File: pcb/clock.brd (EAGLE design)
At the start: 145 x 50 mm, 72 parts, among them IC1 STM32F072C8T6, IC2 REG1117, IC3 24C64ST, U1 DS18B20, X3 USB-MICROB

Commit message: added bom
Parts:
- removed C10, C4, C5, C9: (no value), clock:C1210
- C1, C6, C7, C8: value (none) -> 100nF
- C11, C12: value (none) -> 20p
- C13, C14, C2: value (none) -> 47uF
- C17, C3: value (none) -> 20pF
- L1: value (none) -> 33nH
- R1, R13, R16, R17, R2, R3, R7, R8, R9: value (none) -> 4K7
- R11, R12, R4: value (none) -> 10
- R14, R15, R5: value (none) -> 100
- X2: value (none) -> 32.768KHz
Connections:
- net +3V3: no longer C10.1, C4.1, C5.1, C9.1
- net GND: no longer C10.2, C4.2, C5.2, C9.2
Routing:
- net +3V3: track 78.4 -> 70.3 mm, vias 18 -> 14

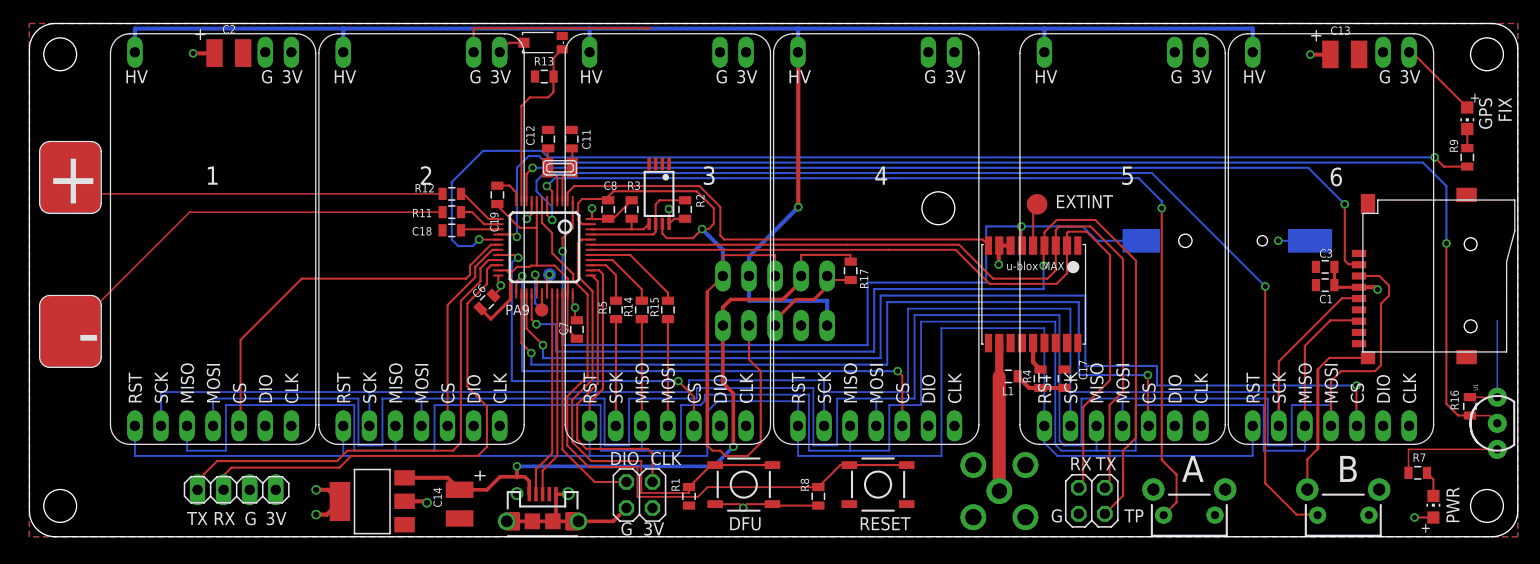
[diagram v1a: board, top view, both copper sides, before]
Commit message: updated to USBC connector
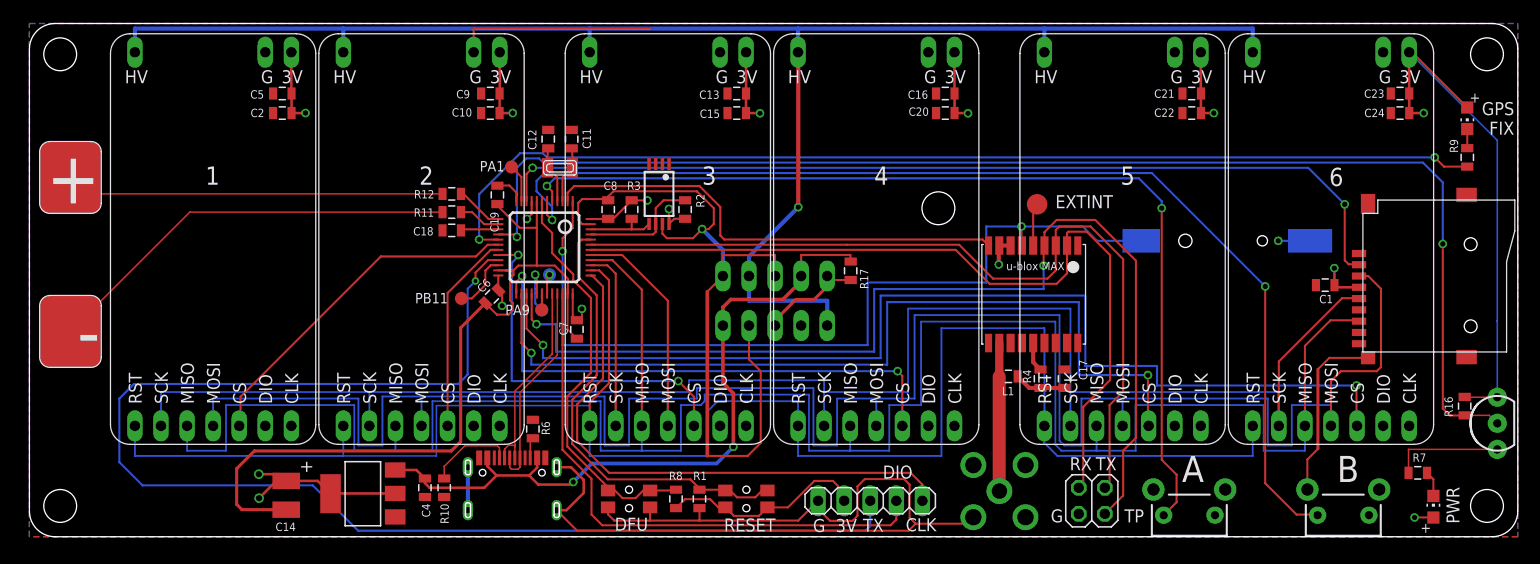
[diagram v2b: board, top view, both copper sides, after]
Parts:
- removed C3: 20pF, clock:0805
- removed JP3: (no value), pinhead:2X02
- removed JP5: (no value), pinhead:1X04
- removed R13: 4K7, clock:0805
- removed R14, R15, R5: 100, clock:0805
- removed S1, S2: TAC_SWITCHSMD, SparkFun-Retired:TACTILE-SWITCH-SMD
- removed U$8: TEMT6000, ProtoSnap-v14a:TEMT6000-SEN
- removed X3: USB-MICROB, basicBoard:USB-MICROB
- added C10, C15, C20, C22, C24, C4, C5: 100nF, clock:0805
- added C16, C21, C23, C9: 10uF, clock:0805
- added JP6: (no value), pinhead:1X05
- added R10, R6: 5.1K, joyAnalog:0805
- added SW1, SW4: 324_SW324_SWITCH_FOOT_HOLE, 3pos_slide_switch:342_SWICH_FOOT_HOLE
- added TP5, TP6: TEST-POINT3X5, SparkFun-Passives:PAD.03X.05
- added U2: USBC_16P, my_usbc_16p:USBC_16P_FOOT
- C13, C2: value 47uF -> 10uF; device clock:C1210 -> clock:0805
- moved C13 59.4 mm to (68.9, 43.2), turned to 180 degrees
- moved C14 16.9 mm to (25.0, 4.04)
- moved R8 13.9 mm to (63.0, 3.68)
- moved C2 7.83 mm to (24.6, 41.3), turned to 180 degrees
- moved IC2 1.19 mm to (32.5, 4.19)
- moved R1 1.05 mm to (65.3, 3.68)
- moved C6 0.72 mm to (45.1, 23.4)
- moved R16 0.51 mm to (139.8, 12.7)
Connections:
- removed net LIGHT_SENSOR_OUTPUT: IC1.11, R13.2, U$8.EMITTER
- removed net N$17: IC1.39, R5.1
- removed net N$19: IC1.41, R15.1
- removed net N$20: IC1.40, R14.1
- removed net PB10: IC1.21, JP5.1
- removed net PB11: IC1.22, JP5.2
- new net N$16: IC1.21, JP6.3
- new net N$22: IC1.22, TP5.P$1
- new net N$23: IC1.11, TP6.P$1
- new net N$31: R6.1, U2.B5
- new net N$33: R10.1, U2.A5
- net +3V3: now also C10.1, C14.1, C15.1, C16.1, C20.1, C21.1, C22.1, C23.1, C24.1, C5.1, C9.1, JP6.2, SW1.P$1, SW1.P$4; no longer C3.1, JP3.3, JP5.4, S1.3, S1.4, U$8.COLLECTOR
- net +5V: now also C4.1, U2.A4B9, U2.B4A9; no longer C14.1, X3.VBUS
- net GND: now also C10.2, C15.2, C16.2, C20.2, C21.2, C22.2, C23.2, C24.2, C4.2, C5.2, C9.2, JP6.1, R10.2, R6.2, SW4.P$1, SW4.P$4, U2.A1B12, U2.B11A12, U2.P$13, U2.P$14, U2.P$15, U2.P$16; no longer C3.2, JP3.1, JP5.3, R13.1, S2.3, S2.4, X3.GND, X3.P1, X3.P2, X3.P3, X3.P4, X3.P5, X3.P6
- net N$3: now also SW4.P$2, SW4.P$3; no longer S2.1, S2.2
- net N$5: now also SW1.P$2, SW1.P$3; no longer S1.1, S1.2
- net SPI1_MISO: now also IC1.40; no longer R14.2
- net SPI1_MOSI: now also IC1.41; no longer R15.2
- net SPI1_SCK: now also IC1.39; no longer R5.2
- net SWCLK: now also JP6.5; no longer JP3.4
- net SWDIO: now also JP6.4; no longer JP3.2
- net USB_DM: now also U2.A7, U2.B7; no longer X3.D-
- net USB_DP: now also U2.A6, U2.B6; no longer X3.D+
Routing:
- net N$16: track 0.00 -> 132.6 mm, vias 0 -> 1
- net GND: track 174.9 -> 302.3 mm
- net +3V3: track 70.3 -> 157.7 mm, vias 14 -> 16
- net PB11: track 48.3 -> 0.00 mm
- net PB10: track 47.9 -> 0.00 mm
- net SWDIO: track 22.8 -> 54.9 mm
- net SWCLK: track 27.9 -> 54.7 mm
- net N$3: track 64.6 -> 40.0 mm
- net LIGHT_SENSOR_OUTPUT: track 17.5 -> 0.00 mm
- net SPI1_MOSI: track 219.0 -> 229.6 mm
- net SPI1_MISO: track 210.1 -> 220.0 mm
- net N$19: track 9.82 -> 0.00 mm
- net N$33: track 0.00 -> 8.46 mm
- net EXIXE_RESET: track 171.5 -> 178.9 mm
- net N$20: track 7.27 -> 0.00 mm
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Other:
- board text added: "PA1"
- board text added: "PB11"
- board text added: "exixe clock PT3 JUL19 dekuNukem"

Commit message: moved header
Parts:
- moved JP6 3.30 mm to (78.6, 3.51)
- moved R8 1.63 mm to (61.4, 3.68)
- moved SW1 1.52 mm to (68.3, 3.68)
- moved SW4 1.52 mm to (56.9, 3.68)
- moved R1 1.45 mm to (63.8, 3.71)
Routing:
- net GND: track 302.3 -> 277.5 mm
- net SWCLK: track 54.7 -> 51.4 mm
- net N$16: track 132.6 -> 129.6 mm
- net SWDIO: track 54.9 -> 52.7 mm
- net N$5: track 44.3 -> 43.5 mm
- net N$3: track 40.0 -> 39.3 mm

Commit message: clean up
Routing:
- net EXIXE1_CS: track 34.1 -> 36.6 mm
- net GND: track 277.5 -> 276.2 mm
- net +3V3: track 157.3 -> 156.7 mm
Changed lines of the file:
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@@
 <text x="79.756" y="5.588" size="1.27" layer="25">DIO</text>
 <text x="85.471" y="1.778" size="1.27" layer="25" rot="R180">CLK</text>
-<text x="71.6534" y="1.7526" size="1.27" layer="25" rot="R180">RESET</text>
+<text x="71.3486" y="1.8034" size="1.27" layer="25" rot="R180">RESET</text>
 <text x="58.5724" y="1.8034" size="1.27" layer="25" rot="R180">DFU</text>
 <text x="100.711" y="2.667" size="1.27" layer="25" rot="R180">G</text>
@@
 <contactref element="SW4" pad="P$4"/>
 <contactref element="JP6" pad="1"/>
-<wire x1="78.0796" y1="5.6134" x2="81.915" y2="5.6134" width="0.2032" layer="1"/>
-<wire x1="78.0796" y1="5.6134" x2="77.3684" y2="4.9022" width="0.2032" layer="1"/>
+<wire x1="77.3684" y1="4.9022" x2="78.0796" y2="5.6134" width="0.2032" layer="1"/>
 <wire x1="77.3684" y1="2.032" x2="76.8858" y2="1.5494" width="0.2032" layer="1"/>
 <wire x1="76.8858" y1="1.5494" x2="74.7014" y2="1.5494" width="0.2032" layer="1"/>
@@
 <wire x1="91.96" y1="1.905" x2="90.6392" y2="0.5842" width="0.2032" layer="1"/>
 <wire x1="90.6392" y1="0.5842" x2="82.3976" y2="0.5842" width="0.2032" layer="1"/>
-<wire x1="79.8576" y1="0.5842" x2="53.3645" y2="0.5842" width="0.2032" layer="1"/>
+<wire x1="82.3976" y1="0.5842" x2="53.3645" y2="0.5842" width="0.2032" layer="1"/>
 <wire x1="81.915" y1="5.6134" x2="82.3976" y2="5.1308" width="0.2032" layer="1"/>
 <wire x1="82.3976" y1="5.1308" x2="82.3976" y2="0.5842" width="0.2032" layer="1"/>
 <wire x1="61.666" y1="30.476" x2="61.666" y2="29.52" width="0.2032" layer="1"/>
-<wire x1="78.0796" y1="5.6134" x2="79.375" y2="5.6134" width="0.2032" layer="1"/>
-<wire x1="82.3976" y1="0.5842" x2="79.8576" y2="0.5842" width="0.2032" layer="1"/>
+<wire x1="78.0796" y1="5.6134" x2="81.915" y2="5.6134" width="0.2032" layer="1"/>
 </signal>
 <signal name="+3V3">
@@
 <via x="22.3774" y="3.7592" extent="1-16" drill="0.6"/>
 <via x="53.8226" y="22.1996" extent="1-16" drill="0.5"/>
-<wire x1="53.1622" y1="21.2708" x2="53.34" y2="21.093" width="0.1778" layer="1"/>
 <via x="60.198" y="32.766" extent="1-16" drill="0.5"/>
-<wire x1="54.864" y1="30.948" x2="54.682" y2="30.948" width="0.2032" layer="1"/>
-<wire x1="54.864" y1="30.948" x2="56.359" y2="30.948" width="0.2032" layer="1"/>
+<wire x1="54.682" y1="30.948" x2="56.359" y2="30.948" width="0.2032" layer="1"/>
 <wire x1="56.359" y1="30.948" x2="56.388" y2="30.977" width="0.2032" layer="1"/>
 <wire x1="56.388" y1="30.977" x2="56.874" y2="30.977" width="0.2032" layer="1"/>
@@
 <wire x1="62.2918" y1="3.7084" x2="61.3664" y2="2.783" width="0.2032" layer="1"/>
 <wire x1="76.073" y1="3.5052" x2="76.073" y2="4.9784" width="0.2032" layer="1"/>
-<wire x1="76.073" y1="4.9784" x2="75.2602" y2="5.7912" width="0.2032" layer="1"/>
-<wire x1="73.0504" y1="5.7912" x2="75.2602" y2="5.7912" width="0.2032" layer="1"/>
+<wire x1="76.073" y1="4.9784" x2="75.438" y2="5.6134" width="0.2032" layer="1"/>
+<wire x1="72.8726" y1="5.6134" x2="75.438" y2="5.6134" width="0.2032" layer="1"/>
 <wire x1="25.019" y1="5.4386" x2="24.0568" y2="5.4386" width="0.254" layer="1"/>
 <wire x1="24.0568" y1="5.4386" x2="22.3774" y2="3.7592" width="0.254" layer="1"/>
@@
 <wire x1="60.198" y1="32.766" x2="58.685" y2="32.766" width="0.2032" layer="1"/>
 <wire x1="58.685" y1="32.766" x2="58.674" y2="32.777" width="0.2032" layer="1"/>
-<wire x1="53.8226" y1="22.1996" x2="53.8226" y2="21.093" width="0.2032" layer="1"/>
-<wire x1="53.8226" y1="21.093" x2="53.34" y2="21.093" width="0.2032" layer="1"/>
-<wire x1="52.932" y1="23.698" x2="52.932" y2="21.501" width="0.2032" layer="1"/>
-<wire x1="52.932" y1="21.501" x2="53.34" y2="21.093" width="0.2032" layer="1"/>
 <wire x1="68.9102" y1="3.683" x2="67.7672" y2="3.683" width="0.2032" layer="1"/>
 <wire x1="72.1106" y1="3.5814" x2="72.1106" y2="4.8514" width="0.2032" layer="1"/>
@@
 <wire x1="67.7672" y1="3.683" x2="66.9422" y2="2.858" width="0.2032" layer="1"/>
 <wire x1="66.9422" y1="2.858" x2="66.276" y2="2.858" width="0.2032" layer="1"/>
-<wire x1="72.1106" y1="4.8514" x2="73.0504" y2="5.7912" width="0.2032" layer="1"/>
+<wire x1="72.1106" y1="4.8514" x2="72.8726" y2="5.6134" width="0.2032" layer="1"/>
 <wire x1="143.002" y1="38.618" x2="143.002" y2="13.589" width="0.1524" layer="16"/>
+<wire x1="52.932" y1="23.698" x2="52.932" y2="21.501" width="0.2032" layer="1"/>
+<wire x1="52.932" y1="21.501" x2="53.34" y2="21.093" width="0.2032" layer="1"/>
+<wire x1="53.8226" y1="22.1996" x2="53.8226" y2="21.5756" width="0.2032" layer="1"/>
+<wire x1="53.8226" y1="21.5756" x2="53.34" y2="21.093" width="0.2032" layer="1"/>
 </signal>
 <signal name="N$27">
@@
 <wire x1="56.4134" y1="5.588" x2="63.8302" y2="5.588" width="0.2032" layer="1"/>
 <wire x1="63.8302" y1="5.588" x2="63.8302" y2="4.6084" width="0.2032" layer="1"/>
-<wire x1="69.2452" y1="5.6388" x2="70.376" y2="4.508" width="0.2032" layer="1"/>
-<wire x1="69.2452" y1="5.6388" x2="67.4068" y2="5.6388" width="0.2032" layer="1"/>
-<wire x1="63.8302" y1="4.6084" x2="66.1756" y2="4.6084" width="0.1524" layer="1"/>
-<wire x1="66.1756" y1="4.6084" x2="66.276" y2="4.508" width="0.1524" layer="1"/>
-<wire x1="67.4068" y1="5.6388" x2="66.276" y2="4.508" width="0.1524" layer="1"/>
+<wire x1="69.2706" y1="5.6134" x2="70.376" y2="4.508" width="0.2032" layer="1"/>
+<wire x1="67.3814" y1="5.6134" x2="69.2706" y2="5.6134" width="0.2032" layer="1"/>
+<wire x1="63.8302" y1="4.6084" x2="66.1756" y2="4.6084" width="0.2032" layer="1"/>
+<wire x1="66.1756" y1="4.6084" x2="66.276" y2="4.508" width="0.2032" layer="1"/>
+<wire x1="66.276" y1="4.508" x2="67.3814" y2="5.6134" width="0.2032" layer="1"/>
 </signal>
 <signal name="+5V">
@@
 <contactref element="U$1" pad="CS"/>
 <wire x1="45.682" y1="28.448" x2="44.6532" y2="28.448" width="0.2032" layer="1"/>
-<wire x1="44.6532" y1="28.448" x2="43.5102" y2="27.305" width="0.2032" layer="1"/>
-<wire x1="43.5102" y1="27.305" x2="34.2392" y2="27.305" width="0.2032" layer="1"/>
-<wire x1="34.2392" y1="27.305" x2="20.574" y2="13.6398" width="0.2032" layer="1"/>
-<wire x1="20.574" y1="13.6398" x2="20.574" y2="10.934" width="0.2032" layer="1"/>
+<wire x1="44.6532" y1="28.448" x2="40.1574" y2="23.9522" width="0.2032" layer="1"/>
+<wire x1="40.1574" y1="23.9522" x2="26.7208" y2="23.9522" width="0.2032" layer="1"/>
+<wire x1="26.7208" y1="23.9522" x2="20.574" y2="17.8054" width="0.2032" layer="1"/>
+<wire x1="20.574" y1="17.8054" x2="20.574" y2="10.934" width="0.2032" layer="1"/>
 <wire x1="20.574" y1="10.934" x2="20.44" y2="10.8" width="0.2032" layer="1"/>
 </signal>
@@
 <wire x1="48.932" y1="21.172" x2="49.403" y2="20.701" width="0.2032" layer="1"/>
 <via x="49.403" y="20.701" extent="1-16" drill="0.5"/>
-<wire x1="49.403" y1="20.701" x2="51.308" y2="20.701" width="0.2032" layer="16"/>
-<wire x1="51.308" y1="20.701" x2="51.308" y2="18.034" width="0.2032" layer="16"/>
-<wire x1="51.308" y1="18.034" x2="82.296" y2="18.034" width="0.2032" layer="16"/>
+<wire x1="49.403" y1="20.701" x2="51.1302" y2="20.701" width="0.2032" layer="16"/>
+<wire x1="51.1302" y1="20.701" x2="51.1302" y2="18.034" width="0.2032" layer="16"/>
+<wire x1="51.1302" y1="18.034" x2="82.296" y2="18.034" width="0.2032" layer="16"/>
 <wire x1="82.296" y1="18.034" x2="82.296" y2="24.13" width="0.2032" layer="16"/>
 <wire x1="82.296" y1="24.13" x2="98.806" y2="24.13" width="0.2032" layer="16"/>
